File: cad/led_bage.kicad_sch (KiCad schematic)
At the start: 3230 parts, among them J1 Conn_01x08_Socket, J2 Conn_01x08_Socket, Q2 AO4407A, U2 74AHCT1G125, U3 74AHCT1G125, U4 74AHCT1G125, U5 74AHCT1G125, U6 74AHCT1G125, U7 74AHCT1G125, U8 74AHCT1G125, U9 74AHCT1G125

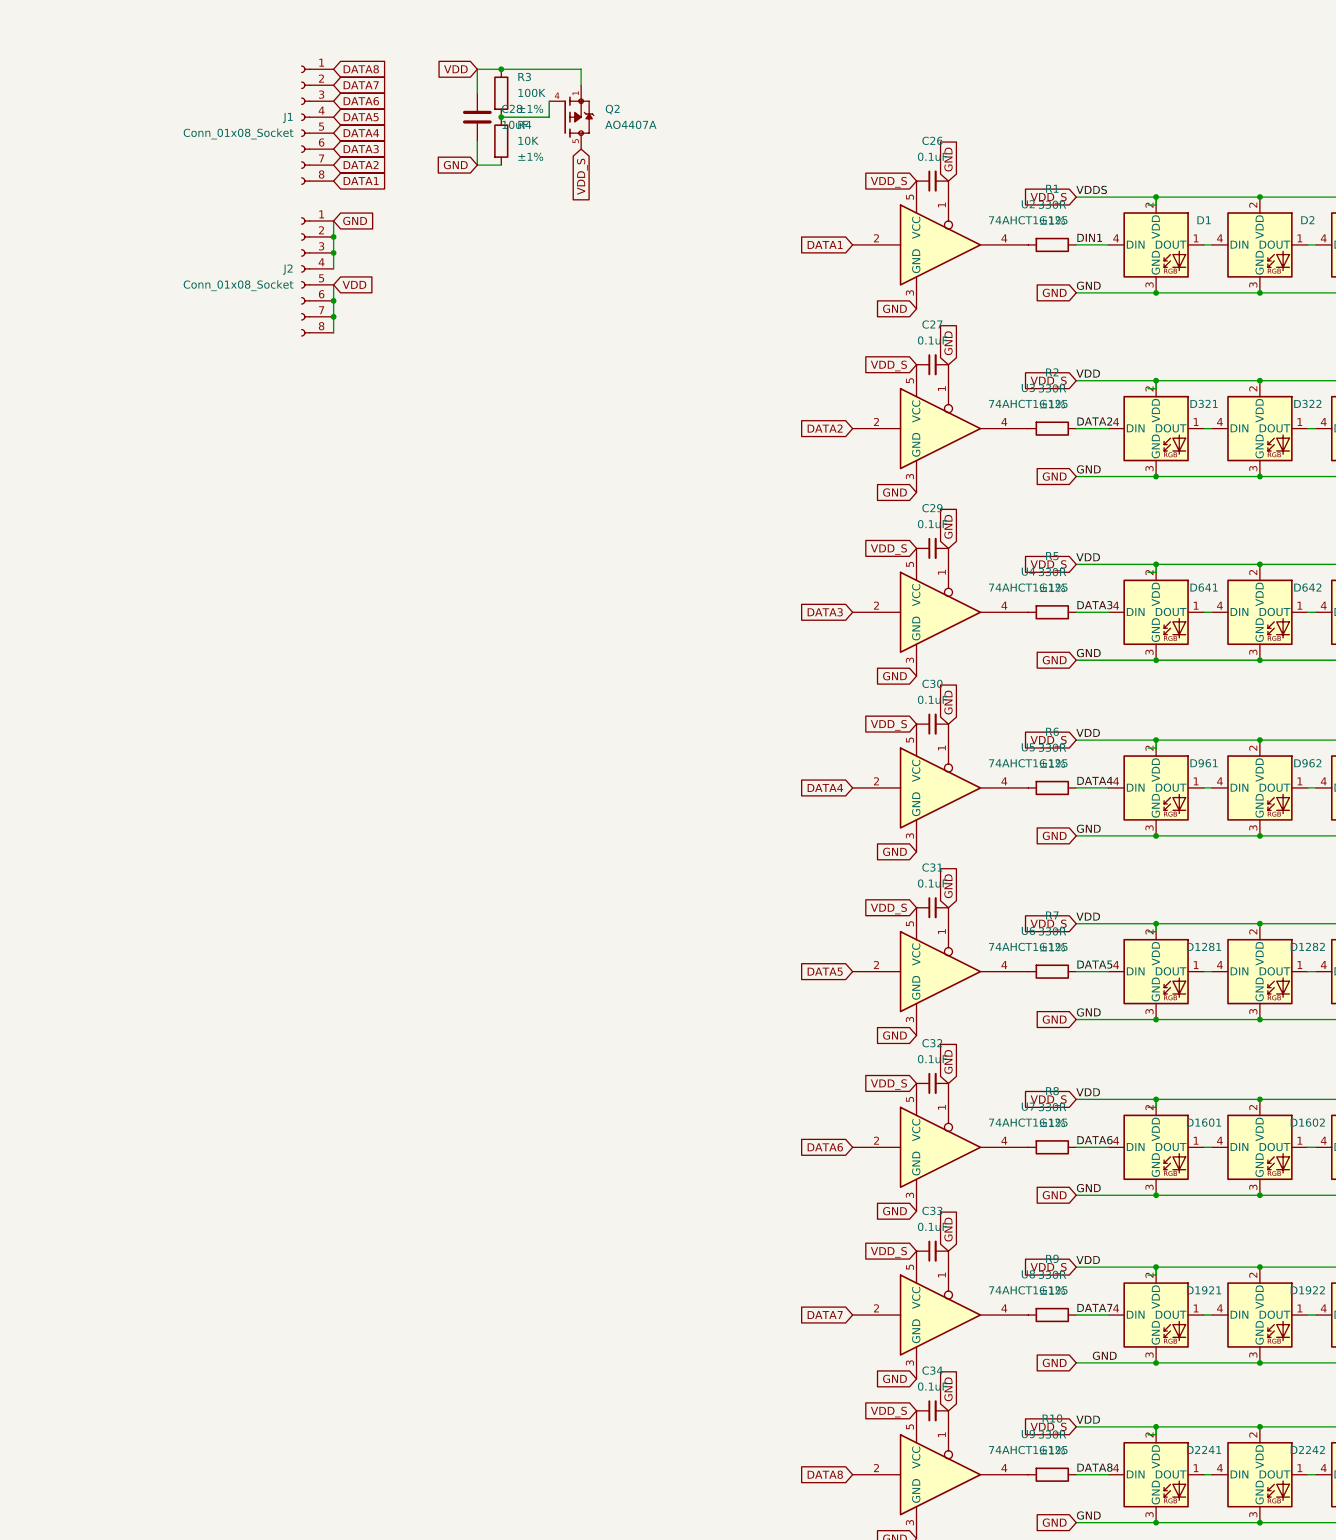
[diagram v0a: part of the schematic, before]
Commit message: feat: scale protection circuit toward 2500-LED main board
Add Si7145DP P-FET (U1) and SnapEDA-imported library table (fp-lib-table)
to the main board. WIP: U1 pin-to-net mapping is incorrect — drain pads
currently land on VDD instead of VDD_S, so the FET is shorted across
itself and not actually protecting anything yet.

Add three pcbnew automation scripts to support the build:
- stitch_power_planes.py: checkerboard via stitching across In1.Cu/In2.Cu
- add_thermal_vias.py: drops thermal via grid under exposed pads
- place_bulk_caps.py: clones a template cap across the LED bbox

Sample board updated alongside the main board for prototyping continuity.
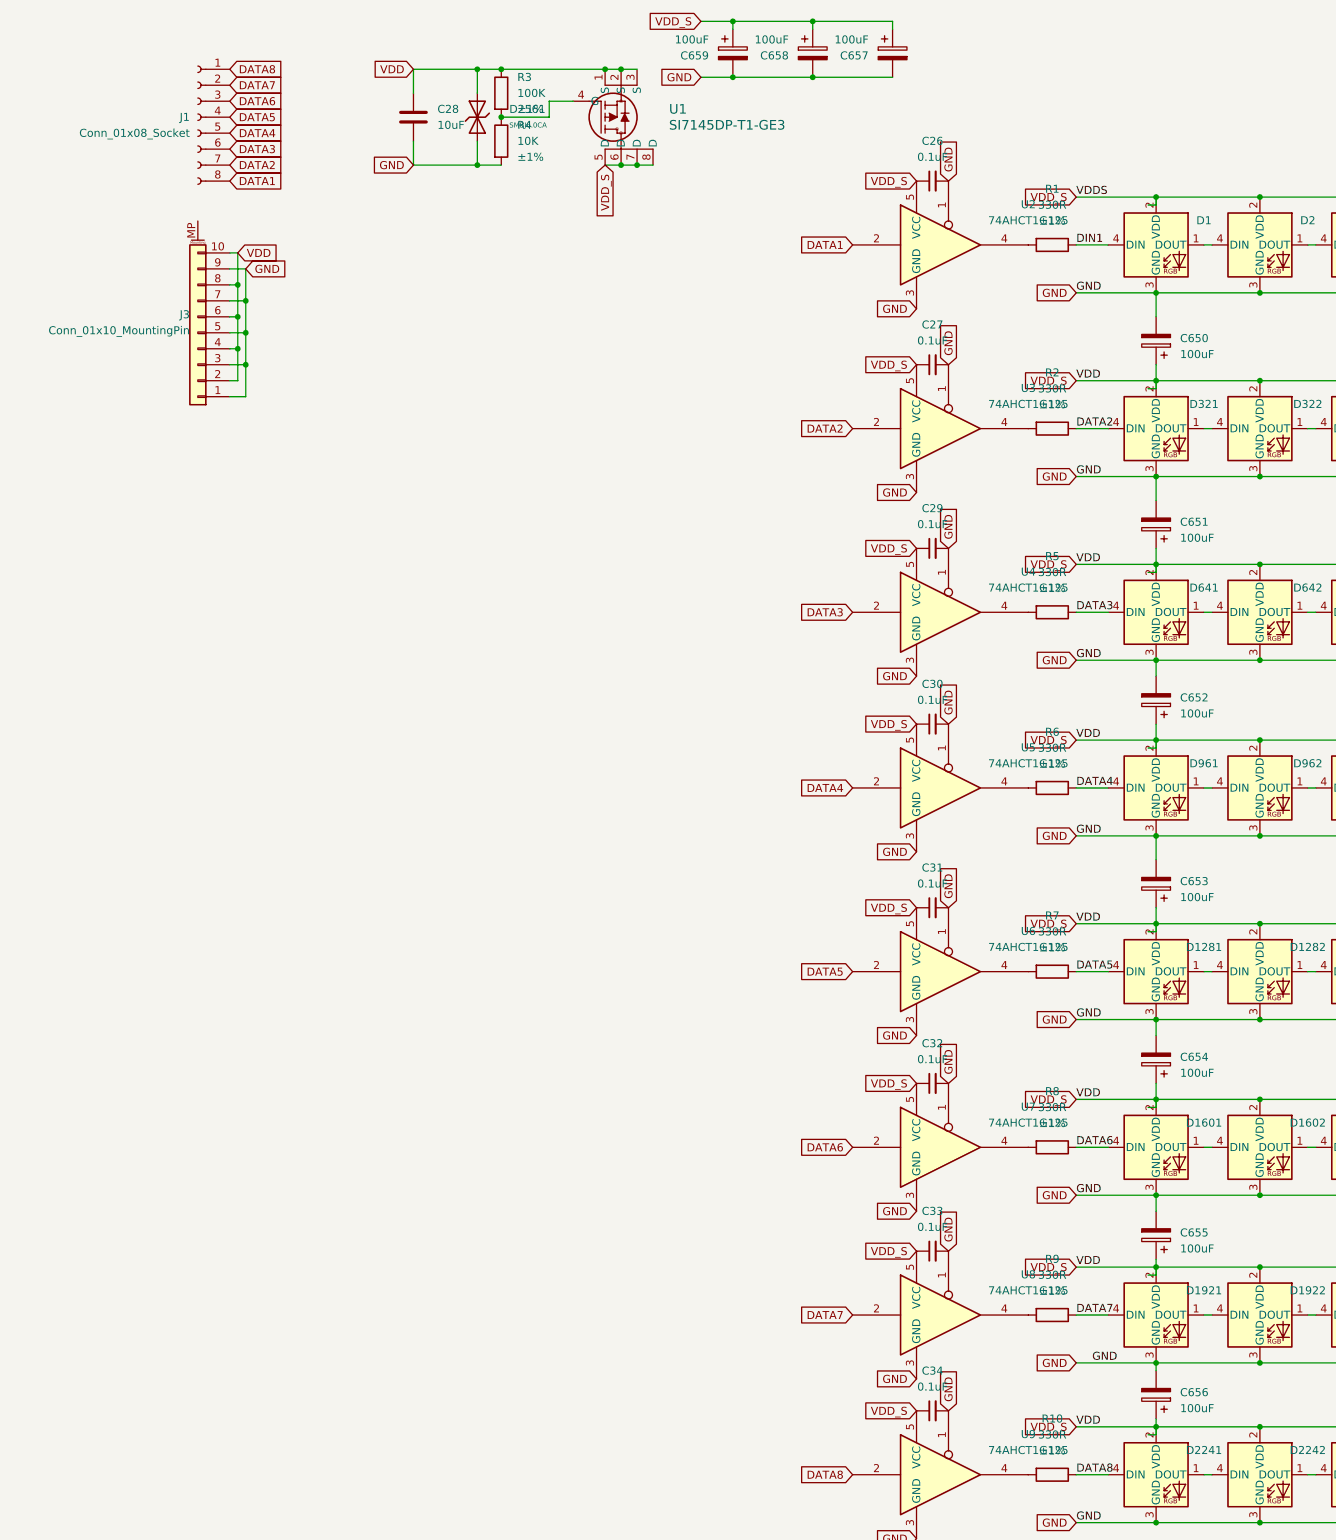
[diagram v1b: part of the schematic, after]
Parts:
- removed J2: Conn_01x08_Socket, Connector_Molex:Molex_CLIK-Mate_502443-0870_1x08-1MP_P2.00mm_Vertical, symbol Connector:Conn_01x08_Socket
- removed Q2: AO4407A, AO4407A:SOIC127P600X175-8N, symbol AO4407A:AO4407A
- added C650, C651, C652, C653, C654, C655, C656, C657, C658, C659: CSH0605-101M1CT, Capacitor_SMD:C_Elec_6.3x5.4, symbol Capacitor_Electrolytic:CSH0605-101M1CT
- added D2561: SMBJ6.0CA, PCM_JLCPCB:D_SMB, symbol JLCPCB-Diodes:TVS-Bi,SMBJ6.0CA
- added J3: Conn_01x10_MountingPin, symbol Connector_Generic_MountingPin:Conn_01x10_MountingPin
- added U1: SI7145DP-T1-GE3, footprints:SON8_SI7135DP-T1-GE3_VIS-L, symbol 2026-04-28_18-53-12:SI7145DP-T1-GE3
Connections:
- net GND: now also C650.2, C651.2, C652.2, C653.2, C654.2, C655.2, C656.2, C657.2, C658.2, C659.2, D2561.1, J3.1 (Pin_1), J3.3 (Pin_3), J3.5 (Pin_5), J3.7 (Pin_7), J3.9 (Pin_9)
- net VDD: now also C650.1, C651.1, C652.1, C653.1, C654.1, C655.1, C656.1, C657.1, C658.1, C659.1, D2561.2, J3.10 (Pin_10), J3.2 (Pin_2), J3.4 (Pin_4), J3.6 (Pin_6), J3.8 (Pin_8), U1.1 (S), U1.2 (S), U1.3 (S), U1.5 (D), U1.6 (D), U1.7 (D), U1.8 (D)
- net at R3.2, R4.1: now also U1.4 (G)
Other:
- moved on the sheet: C28, J1
